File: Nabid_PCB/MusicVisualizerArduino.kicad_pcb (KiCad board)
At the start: 2 copper layers, 94 x 50.8 mm, 23 parts, among them J3 Power_BarrelJack, J4 RGB_STRIP, U1 MSGEQ7, U2 MSGEQ7

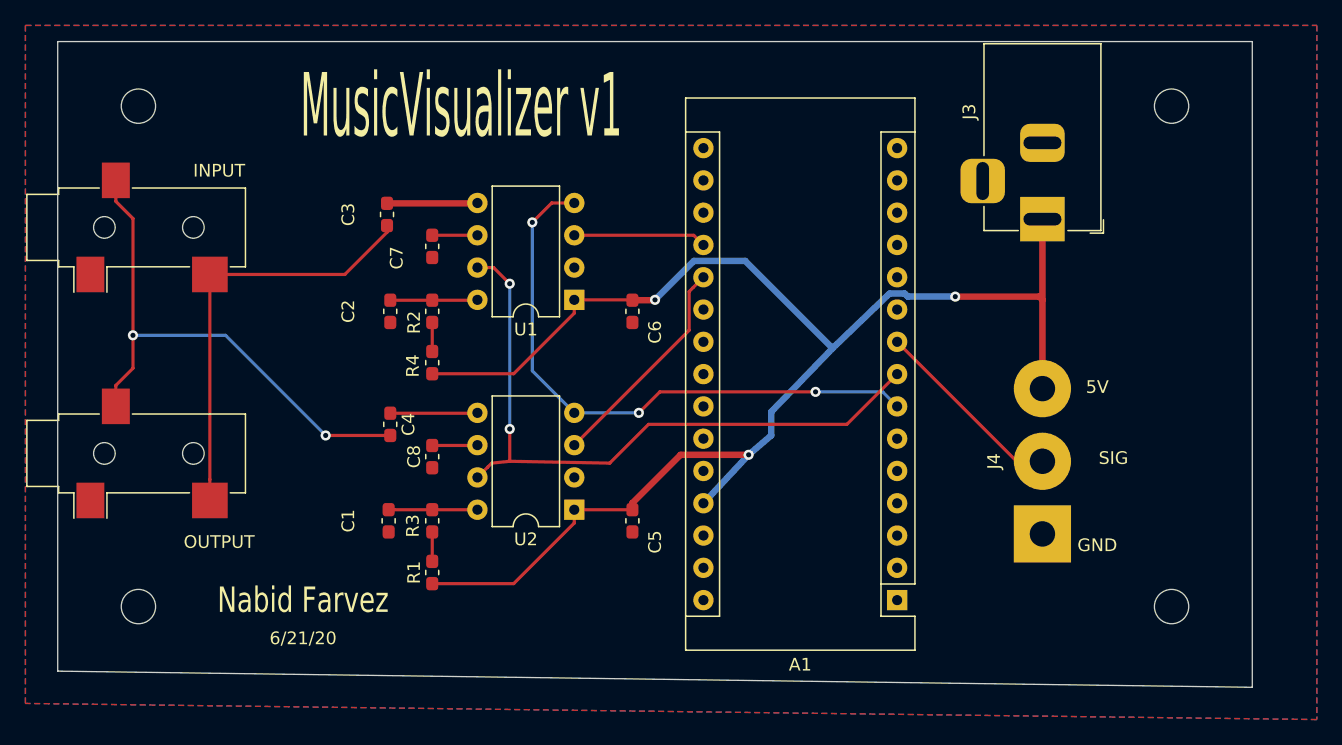
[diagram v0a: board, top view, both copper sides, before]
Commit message: fixed board cut outline alignment
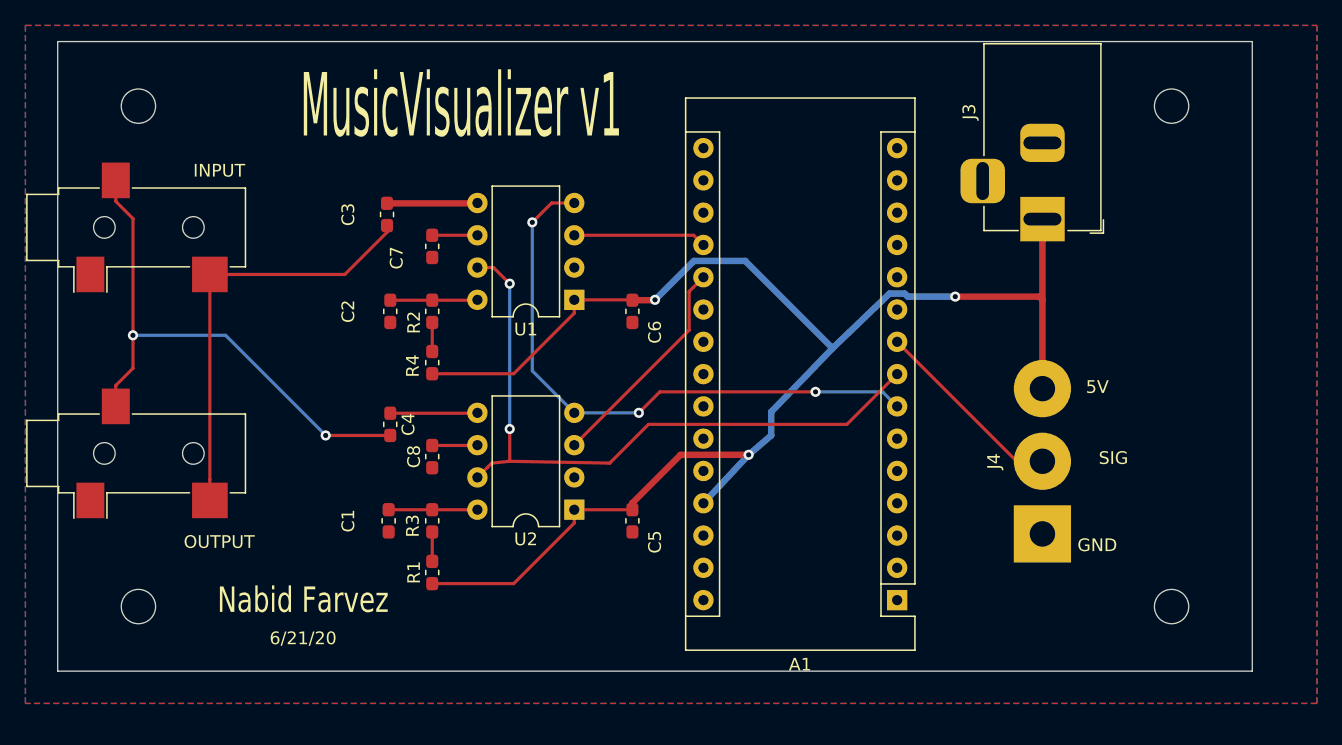
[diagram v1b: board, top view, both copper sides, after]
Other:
- board size 94 x 50.8 mm -> 94 x 49.5 mm
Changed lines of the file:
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@@
   )
   (gr_line (start 68.58 90.17) (end 68.58 40.64) (layer Edge.Cuts) (width 0.05))
-  (gr_line (start 162.56 91.44) (end 68.58 90.17) (layer Edge.Cuts) (width 0.05))
-  (gr_line (start 162.56 40.64) (end 162.56 91.44) (layer Edge.Cuts) (width 0.05))
+  (gr_line (start 162.56 90.17) (end 68.58 90.17) (layer Edge.Cuts) (width 0.05))
+  (gr_line (start 162.56 40.64) (end 162.56 90.17) (layer Edge.Cuts) (width 0.05))
   (gr_line (start 68.58 40.64) (end 162.56 40.64) (layer Edge.Cuts) (width 0.05))
   (segment (start 118.618 55.88) (end 119.38 56.642) (width 0.25) (layer F.Cu) (net 6))
@@
     (polygon
       (pts
-        (xy 167.64 93.98) (xy 66.04 92.71) (xy 66.04 39.37) (xy 167.64 39.37)
+        (xy 167.64 92.71) (xy 66.04 92.71) (xy 66.04 39.37) (xy 167.64 39.37)
       )
     )
@@
     (polygon
       (pts
-        (xy 167.64 93.98) (xy 66.04 92.71) (xy 66.04 39.37) (xy 167.64 39.37)
+        (xy 167.64 92.71) (xy 66.04 92.71) (xy 66.04 39.37) (xy 167.64 39.37)
       )
     )
